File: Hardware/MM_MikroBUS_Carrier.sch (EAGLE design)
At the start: 50 parts, among them J15 MICROMOD-2222-C, J2 QWIIC_RIGHT_ANGLE, J5 Vertical Qwiic Connector, J7 MIKROBUS_SMD_BLACK1, U1 MCP73831, U2 AP7361C-33FGEUDFN-8

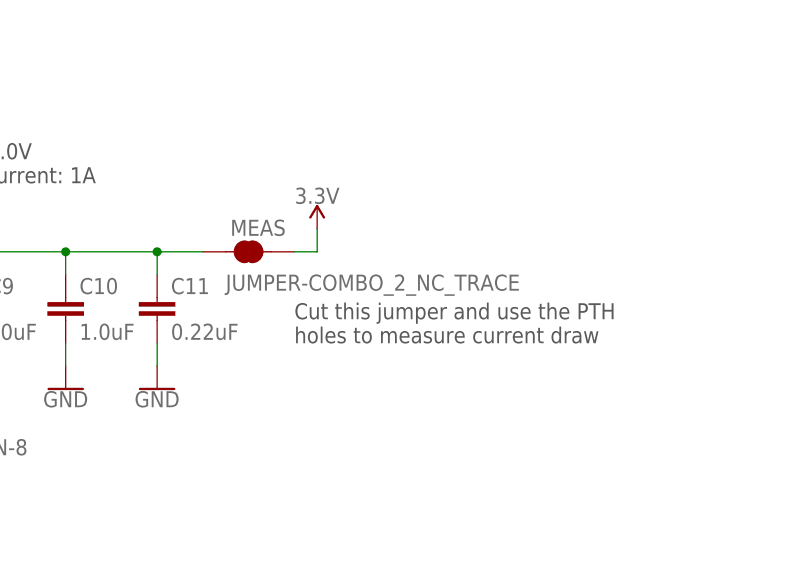
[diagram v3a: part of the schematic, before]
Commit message: Proto checklist
Updated silkscreen and measures
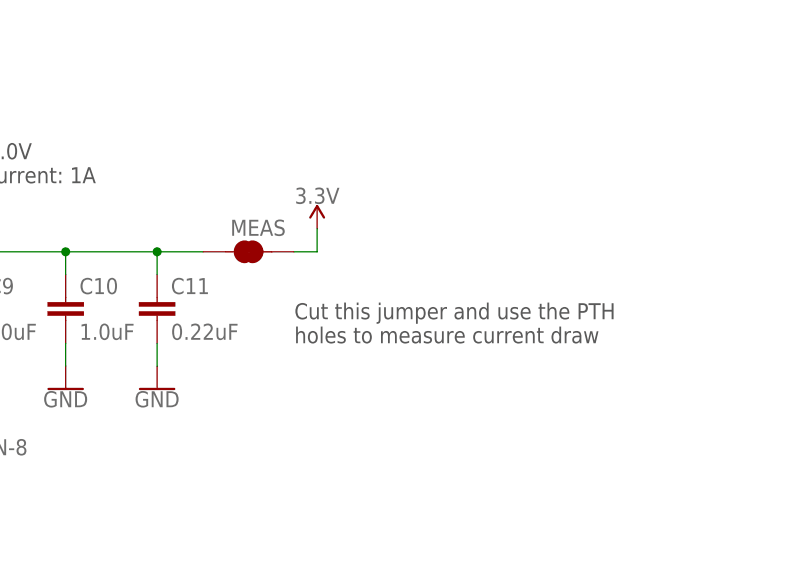
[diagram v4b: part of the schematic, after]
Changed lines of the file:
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@@
 <?xml version="1.0" encoding="utf-8"?>
 <!DOCTYPE eagle SYSTEM "eagle.dtd">
-<eagle version="9.5.2">
+<eagle version="9.4.2">
 <drawing>
 <settings>
-<setting alwaysvectorfont="no"/>
+<setting alwaysvectorfont="yes"/>
 <setting verticaltext="up"/>
 </settings>
@@
 <instance part="MEAS" gate="JP1" x="363.22" y="246.38" smashed="yes">
 <attribute name="NAME" x="361.188" y="248.158" size="1.778" layer="95" font="vector"/>
-<attribute name="VALUE" x="360.68" y="243.84" size="1.778" layer="96" font="vector" align="top-left"/>
 </instance>
 <instance part="GND6" gate="1" x="279.4" y="231.14" smashed="yes">

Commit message: Update schematic
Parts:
- S3: value BOOT -> MIK_RESET
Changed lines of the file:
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@@
 <part name="SUPPLY18" library="SparkFun-PowerSymbols" deviceset="3.3V" device=""/>
 <part name="SUPPLY19" library="SparkFun-PowerSymbols" deviceset="VIN" device=""/>
-<part name="S3" library="SparkFun-Switches" deviceset="MOMENTARY-SWITCH-SPST" device="-SMD-5.2-TALL-REDUNDANT" value="BOOT"/>
+<part name="S3" library="SparkFun-Switches" deviceset="MOMENTARY-SWITCH-SPST" device="-SMD-5.2-TALL-REDUNDANT" value="MIK_RESET"/>
 <part name="GND11" library="SparkFun-PowerSymbols" deviceset="GND" device=""/>
 </parts>
